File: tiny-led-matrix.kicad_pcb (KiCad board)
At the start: 4 copper layers, 89 x 85 mm, 998 parts, among them J1 TagConnect_TC2030_SWD, U1 STM32F030F4Px

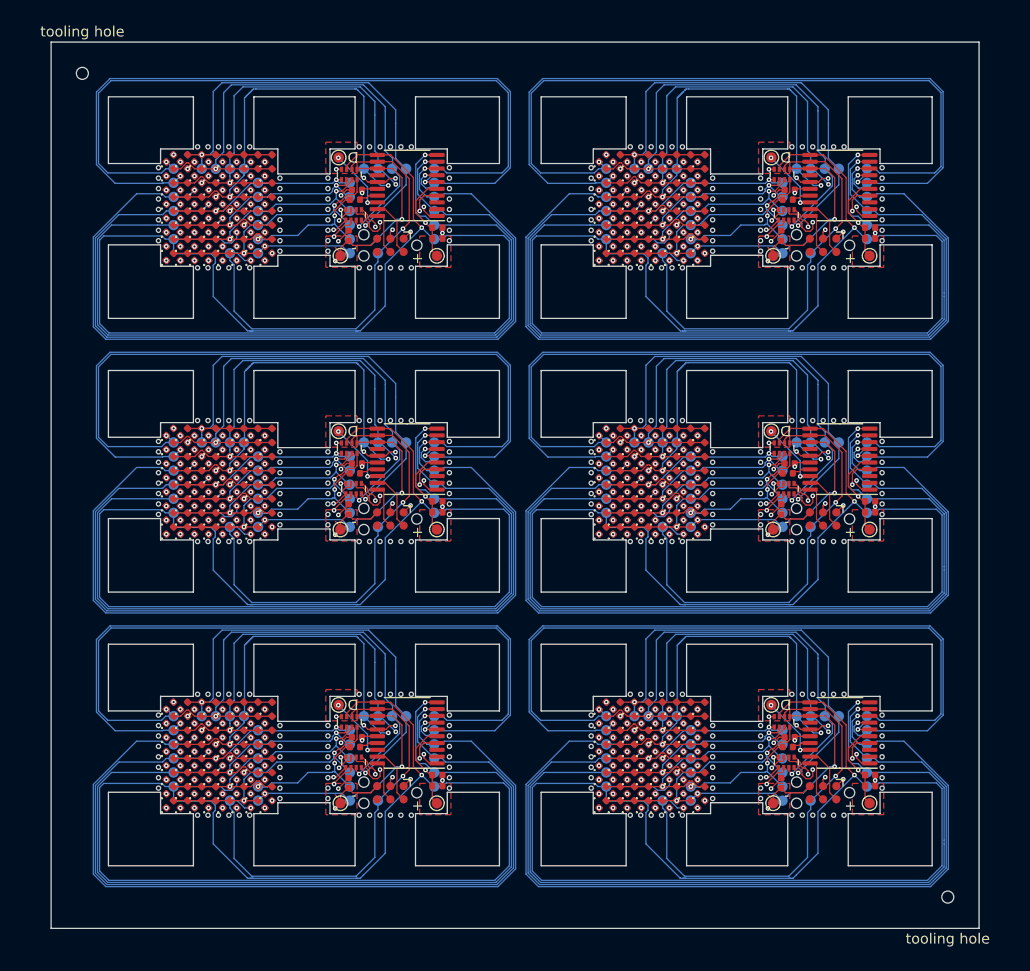
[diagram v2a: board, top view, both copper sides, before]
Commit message: Update board fab settings
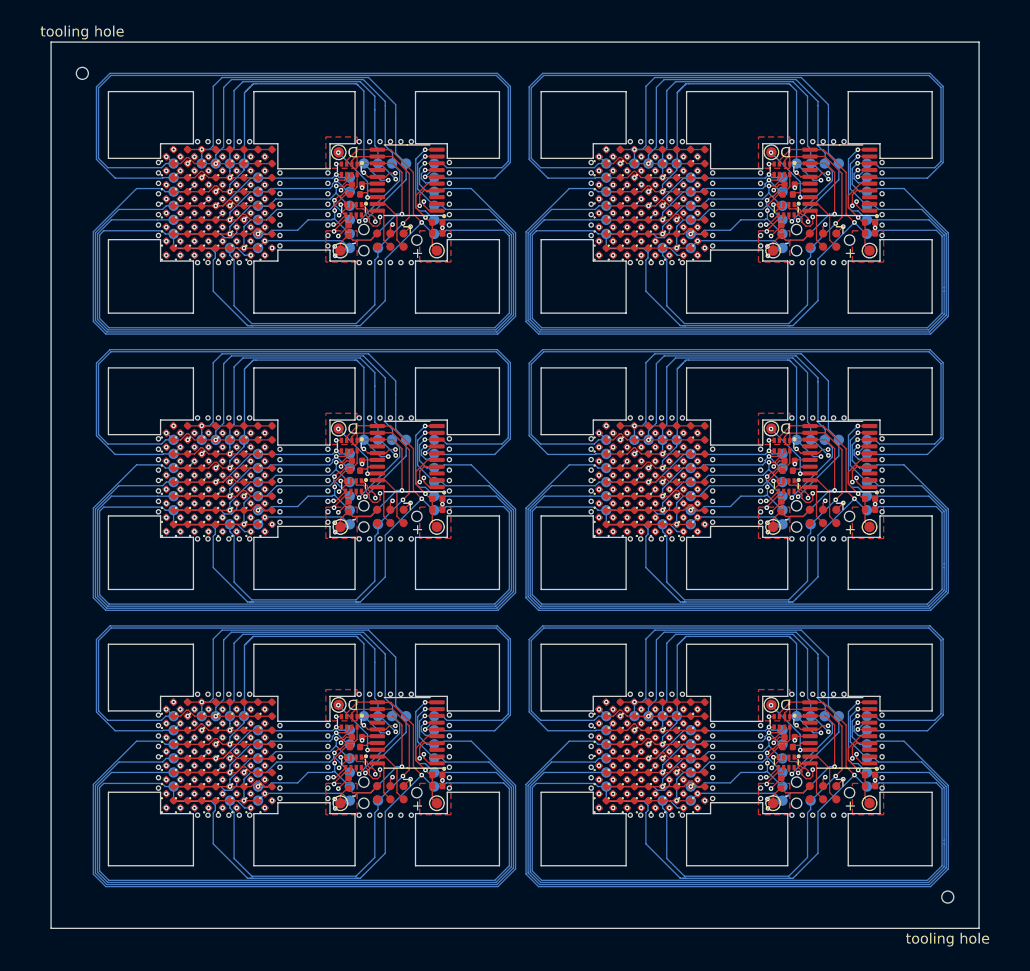
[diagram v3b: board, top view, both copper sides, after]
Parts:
- removed the C1 at (167.2, 81.5)
- removed the C1 at (167.2, 55.2)
- removed the C1 at (125.7, 55.2)
- removed the C1 at (125.7, 81.5)
- removed the C2 at (159.4, 76.8)
- removed the C2 at (159.4, 50.5)
- removed the C2 at (117.9, 50.5)
- removed the C2 at (117.9, 76.8)
- removed the C3 at (167.2, 54.1)
- removed the C3 at (167.2, 80.4)
- removed the C3 at (125.7, 54.1)
- removed the C3 at (125.7, 80.4)
- removed the C4 at (158.6, 81.2)
- removed the C4 at (158.6, 54.9)
- removed the C4 at (117.1, 54.9)
- removed the C4 at (117.1, 81.2)
- removed the D1 at (141.5, 73.8)
- removed the D1 at (141.5, 47.5)
- removed the D1 at (100.0, 47.5)
- removed the D1 at (100.0, 73.8)
- removed the D10 at (142.8, 48.9)
- removed the D10 at (142.8, 75.1)
- removed the D10 at (101.3, 48.9)
- removed the D10 at (101.3, 75.1)
- removed the D11 at (142.8, 50.2)
- removed the D11 at (142.8, 76.5)
- removed the D11 at (101.3, 50.2)
- removed the D11 at (101.3, 76.5)
- removed the D12 at (142.8, 77.8)
- removed the D12 at (142.8, 51.5)
- removed the D12 at (101.3, 51.5)
- removed the D12 at (101.3, 77.8)
- removed the D13 at (142.8, 52.9)
- removed the D13 at (142.8, 79.2)
- removed the D13 at (101.3, 52.9)
- removed the D13 at (101.3, 79.2)
- removed the D14 at (142.8, 54.2)
- removed the D14 at (142.8, 80.5)
- removed the D14 at (101.3, 54.2)
- removed the D14 at (101.3, 80.5)
- removed the D15 at (142.8, 55.6)
- removed the D15 at (142.8, 81.8)
- removed the D15 at (101.3, 55.6)
- removed the D15 at (101.3, 81.8)
- removed the D16 at (142.8, 57.0)
- removed the D16 at (142.8, 83.2)
- removed the D16 at (101.3, 57.0)
- removed the D16 at (101.3, 83.2)
- removed the D17 at (144.2, 47.5)
- removed the D17 at (144.2, 73.8)
- removed the D17 at (102.7, 47.5)
- removed the D17 at (102.7, 73.8)
- removed the D18 at (144.2, 48.9)
- removed the D18 at (144.2, 75.1)
- removed the D18 at (102.7, 48.9)
- removed the D18 at (102.7, 75.1)
- removed the D19 at (144.2, 76.5)
- removed the D19 at (144.2, 50.2)
- removed the D19 at (102.7, 50.2)
- removed the D19 at (102.7, 76.5)
- removed the D2 at (141.5, 75.1)
- removed the D2 at (141.5, 48.9)
- removed the D2 at (100.0, 48.9)
- removed the D2 at (100.0, 75.1)
- removed the D20 at (144.2, 77.8)
- removed the D20 at (144.2, 51.5)
- removed the D20 at (102.7, 51.5)
- removed the D20 at (102.7, 77.8)
- removed the D21 at (144.2, 79.2)
- removed the D21 at (144.2, 52.9)
- removed the D21 at (102.7, 52.9)
- removed the D21 at (102.7, 79.2)
- removed the D22 at (144.2, 54.2)
- removed the D22 at (144.2, 80.5)
- removed the D22 at (102.7, 54.2)
- removed the D22 at (102.7, 80.5)
- removed the D23 at (144.2, 81.8)
- removed the D23 at (144.2, 55.6)
- removed the D23 at (102.7, 55.6)
- removed the D23 at (102.7, 81.8)
- removed the D24 at (144.2, 57.0)
- removed the D24 at (144.2, 83.2)
- removed the D24 at (102.7, 57.0)
- removed the D24 at (102.7, 83.2)
- removed the D25 at (145.6, 73.8)
- removed the D25 at (145.6, 47.5)
- removed the D25 at (104.0, 47.5)
- removed the D25 at (104.0, 73.8)
- removed the D26 at (145.6, 48.9)
- removed the D26 at (145.6, 75.1)
- removed the D26 at (104.0, 48.9)
- removed the D26 at (104.0, 75.1)
- removed the D27 at (145.6, 50.2)
- removed the D27 at (145.6, 76.5)
- removed the D27 at (104.0, 50.2)
- removed the D27 at (104.0, 76.5)
- removed the D28 at (145.6, 77.8)
- removed the D28 at (145.6, 51.5)
- removed the D28 at (104.0, 51.5)
- removed the D28 at (104.0, 77.8)
- removed the D29 at (145.6, 79.2)
- removed the D29 at (145.6, 52.9)
- removed the D29 at (104.0, 52.9)
- removed the D29 at (104.0, 79.2)
- removed the D3 at (141.5, 76.5)
- removed the D3 at (141.5, 50.2)
- removed the D3 at (100.0, 50.2)
- removed the D3 at (100.0, 76.5)
- removed the D30 at (145.6, 80.5)
- removed the D30 at (145.6, 54.2)
- removed the D30 at (104.0, 54.2)
- removed the D30 at (104.0, 80.5)
- removed the D31 at (145.6, 81.8)
- removed the D31 at (145.6, 55.6)
- removed the D31 at (104.0, 55.6)
- removed the D31 at (104.0, 81.8)
- removed the D32 at (145.6, 83.2)
- removed the D32 at (145.6, 57.0)
- removed the D32 at (104.0, 57.0)
- removed the D32 at (104.0, 83.2)
- removed the D33 at (146.9, 73.8)
- removed the D33 at (146.9, 47.5)
- removed the D33 at (105.4, 47.5)
- removed the D33 at (105.4, 73.8)
- removed the D34 at (146.9, 48.9)
- removed the D34 at (146.9, 75.1)
- removed the D34 at (105.4, 48.9)
- removed the D34 at (105.4, 75.1)
- removed the D35 at (146.9, 50.2)
- removed the D35 at (146.9, 76.5)
- removed the D35 at (105.4, 50.2)
- removed the D35 at (105.4, 76.5)
- removed the D36 at (146.9, 77.8)
- removed the D36 at (146.9, 51.5)
- removed the D36 at (105.4, 51.5)
- removed the D36 at (105.4, 77.8)
- removed the D37 at (146.9, 79.2)
- removed the D37 at (146.9, 52.9)
- removed the D37 at (105.4, 52.9)
- removed the D37 at (105.4, 79.2)
- removed the D38 at (146.9, 80.5)
- removed the D38 at (146.9, 54.2)
- removed the D38 at (105.4, 54.2)
- removed the D38 at (105.4, 80.5)
- removed the D39 at (146.9, 81.8)
- removed the D39 at (146.9, 55.6)
- removed the D39 at (105.4, 55.6)
- removed the D39 at (105.4, 81.8)
- removed the D4 at (141.5, 51.5)
- removed the D4 at (141.5, 77.8)
- removed the D4 at (100.0, 51.5)
- removed the D4 at (100.0, 77.8)
- removed the D40 at (146.9, 83.2)
- removed the D40 at (146.9, 57.0)
- removed the D40 at (105.4, 57.0)
- removed the D40 at (105.4, 83.2)
- removed the D41 at (148.2, 47.5)
- removed the D41 at (148.2, 73.8)
- removed the D41 at (106.8, 47.5)
- removed the D41 at (106.8, 73.8)
- removed the D42 at (148.2, 48.9)
- removed the D42 at (148.2, 75.1)
- removed the D42 at (106.8, 48.9)
- removed the D42 at (106.8, 75.1)
- removed the D43 at (148.2, 50.2)
- removed the D43 at (148.2, 76.5)
- removed the D43 at (106.8, 50.2)
- removed the D43 at (106.8, 76.5)
- removed the D44 at (148.2, 77.8)
- removed the D44 at (148.2, 51.5)
- removed the D44 at (106.8, 51.5)
- removed the D44 at (106.8, 77.8)
- removed the D45 at (148.2, 52.9)
- removed the D45 at (148.2, 79.2)
- removed the D45 at (106.8, 52.9)
- removed the D45 at (106.8, 79.2)
- removed the D46 at (148.2, 80.5)
- removed the D46 at (148.2, 54.2)
- removed the D46 at (106.8, 54.2)
- removed the D46 at (106.8, 80.5)
- removed the D47 at (148.2, 81.8)
- removed the D47 at (148.2, 55.6)
- removed the D47 at (106.8, 55.6)
- removed the D47 at (106.8, 81.8)
- removed the D48 at (148.2, 83.2)
- removed the D48 at (148.2, 57.0)
- removed the D48 at (106.8, 57.0)
- removed the D48 at (106.8, 83.2)
- removed the D49 at (149.6, 47.5)
- removed the D49 at (149.6, 73.8)
- removed the D49 at (108.1, 47.5)
- removed the D49 at (108.1, 73.8)
- removed the D5 at (141.5, 52.9)
- removed the D5 at (141.5, 79.2)
- removed the D5 at (100.0, 52.9)
- removed the D5 at (100.0, 79.2)
- removed the D50 at (149.6, 48.9)
- removed the D50 at (149.6, 75.1)
- removed the D50 at (108.1, 48.9)
- removed the D50 at (108.1, 75.1)
- removed the D51 at (149.6, 50.2)
- removed the D51 at (149.6, 76.5)
- removed the D51 at (108.1, 50.2)
- removed the D51 at (108.1, 76.5)
- removed the D52 at (149.6, 51.5)
- removed the D52 at (149.6, 77.8)
- removed the D52 at (108.1, 51.5)
- removed the D52 at (108.1, 77.8)
- removed the D53 at (149.6, 52.9)
- removed the D53 at (149.6, 79.2)
- removed the D53 at (108.1, 52.9)
- removed the D53 at (108.1, 79.2)
- removed the D54 at (149.6, 80.5)
- removed the D54 at (149.6, 54.2)
- removed the D54 at (108.1, 54.2)
- removed the D54 at (108.1, 80.5)
- removed the D55 at (149.6, 81.8)
- removed the D55 at (149.6, 55.6)
- removed the D55 at (108.1, 55.6)
- removed the D55 at (108.1, 81.8)
- removed the D56 at (149.6, 83.2)
- removed the D56 at (149.6, 57.0)
- removed the D56 at (108.1, 57.0)
- removed the D56 at (108.1, 83.2)
- removed the D57 at (150.9, 47.5)
- removed the D57 at (150.9, 73.8)
- removed the D57 at (109.5, 47.5)
- removed the D57 at (109.5, 73.8)
- removed the D58 at (150.9, 48.9)
- removed the D58 at (150.9, 75.1)
- removed the D58 at (109.5, 48.9)
- removed the D58 at (109.5, 75.1)
- removed the D59 at (150.9, 50.2)
- removed the D59 at (150.9, 76.5)
- removed the D59 at (109.5, 50.2)
- removed the D59 at (109.5, 76.5)
- removed the D6 at (141.5, 54.2)
- removed the D6 at (141.5, 80.5)
- removed the D6 at (100.0, 54.2)
- removed the D6 at (100.0, 80.5)
- removed the D60 at (150.9, 77.8)
- removed the D60 at (150.9, 51.5)
- removed the D60 at (109.5, 51.5)
- removed the D60 at (109.5, 77.8)
- removed the D61 at (150.9, 52.9)
- removed the D61 at (150.9, 79.2)
- removed the D61 at (109.5, 52.9)
- removed the D61 at (109.5, 79.2)
- removed the D62 at (150.9, 80.5)
- removed the D62 at (150.9, 54.2)
- removed the D62 at (109.5, 54.2)
- removed the D62 at (109.5, 80.5)
- removed the D63 at (150.9, 81.8)
- removed the D63 at (150.9, 55.6)
- removed the D63 at (109.5, 55.6)
- removed the D63 at (109.5, 81.8)
- removed the D64 at (150.9, 83.2)
- removed the D64 at (150.9, 57.0)
- removed the D64 at (109.5, 57.0)
- removed the D64 at (109.5, 83.2)
- removed the D7 at (141.5, 81.8)
- removed the D7 at (141.5, 55.6)
- removed the D7 at (100.0, 55.6)
- removed the D7 at (100.0, 81.8)
- removed the D8 at (141.5, 57.0)
- removed the D8 at (141.5, 83.2)
- removed the D8 at (100.0, 57.0)
- removed the D8 at (100.0, 83.2)
- removed the D9 at (142.8, 73.8)
- removed the D9 at (142.8, 47.5)
- removed the D9 at (101.3, 47.5)
- removed the D9 at (101.3, 73.8)
- removed the J1 at (162.6, 55.8)
- removed the J1 at (162.6, 82.1)
- removed the J1 at (121.1, 55.8)
- removed the J1 at (121.1, 82.1)
- removed the R1 at (159.2, 77.7)
- removed the R1 at (159.2, 51.5)
- removed the R1 at (117.8, 51.5)
- removed the R1 at (117.8, 77.7)
- removed the REF** at (161.7, 72.7)
- removed the REF** at (162.7, 46.4)
- removed the REF** at (168.3, 52.4)
- removed the REF** at (147.2, 84.2)
- removed the REF** at (163.7, 58.0)
- removed the REF** at (146.2, 46.4)
- removed the REF** at (162.7, 58.0)
- removed the REF** at (163.7, 46.4)
- removed the REF** at (161.7, 46.4)
- removed the REF** at (148.2, 58.0)
- removed the REF** at (160.7, 46.4)
- removed the REF** at (144.2, 46.4)
- removed the REF** at (147.2, 46.4)
- removed the REF** at (161.7, 58.0)
- removed the REF** at (160.7, 58.0)
- removed the REF** at (164.7, 58.0)
- removed the REF** at (159.7, 58.0)
- removed the REF** at (156.7, 81.7)
- removed the REF** at (152.1, 79.7)
- removed the REF** at (140.4, 51.4)
- removed the REF** at (146.2, 58.0)
- removed the REF** at (152.1, 49.4)
- removed the REF** at (152.1, 55.4)
- removed the REF** at (152.1, 54.4)
- removed the REF** at (152.1, 53.4)
- removed the REF** at (152.1, 56.4)
- removed the REF** at (156.7, 76.7)
- removed the REF** at (152.1, 50.4)
- removed the REF** at (152.1, 51.4)
- removed the REF** at (140.4, 81.7)
- removed the REF** at (156.7, 78.7)
- removed the REF** at (168.3, 55.4)
- removed the REF** at (147.2, 58.0)
- removed the REF** at (152.1, 82.7)
- removed the REF** at (164.7, 46.4)
- removed the REF** at (168.3, 50.4)
- removed the REF** at (168.3, 53.4)
- removed the REF** at (145.2, 58.0)
- removed the REF** at (168.3, 48.4)
- removed the REF** at (168.3, 49.4)
- removed the REF** at (152.1, 77.7)
- removed the REF** at (159.7, 46.4)
- removed the REF** at (140.4, 52.4)
- removed the REF** at (140.4, 49.4)
- removed the REF** at (140.4, 50.4)
- removed the REF** at (156.7, 56.4)
- removed the REF** at (156.7, 50.4)
- removed the REF** at (156.7, 51.4)
- removed the REF** at (168.3, 54.4)
- removed the REF** at (140.4, 54.4)
- removed the REF** at (140.4, 55.4)
- removed the REF** at (168.3, 78.7)
- removed the REF** at (156.7, 52.4)
- removed the REF** at (168.3, 51.4)
- removed the REF** at (144.2, 58.0)
- removed the REF** at (156.7, 55.4)
- removed the REF** at (168.3, 77.7)
- removed the REF** at (156.7, 79.7)
- removed the REF** at (159.7, 72.7)
- removed the REF** at (156.7, 80.7)
- removed the REF** at (115.2, 49.4)
- removed the REF** at (126.8, 51.4)
- removed the REF** at (115.2, 52.4)
- removed the REF** at (98.9, 55.4)
- removed the REF** at (98.9, 54.4)
- removed the REF** at (126.8, 54.4)
- removed the REF** at (115.2, 51.4)
- removed the REF** at (115.2, 50.4)
- removed the REF** at (115.2, 56.4)
- removed the REF** at (148.2, 84.2)
- removed the REF** at (98.9, 50.4)
- removed the REF** at (98.9, 49.4)
- removed the REF** at (98.9, 52.4)
- removed the REF** at (118.2, 46.4)
- removed the REF** at (126.8, 49.4)
- removed the REF** at (126.8, 48.4)
- removed the REF** at (103.7, 58.0)
- removed the REF** at (126.8, 50.4)
- removed the REF** at (123.2, 46.4)
- removed the REF** at (107.7, 58.0)
- removed the REF** at (160.7, 72.7)
- removed the REF** at (115.2, 53.4)
- removed the REF** at (115.2, 54.4)
- removed the REF** at (115.2, 55.4)
- removed the REF** at (107.7, 46.4)
- removed the REF** at (98.9, 48.4)
- removed the REF** at (103.7, 46.4)
- removed the REF** at (104.7, 46.4)
- removed the REF** at (122.2, 58.0)
- removed the REF** at (106.7, 46.4)
- removed the REF** at (110.5, 52.4)
- removed the REF** at (144.2, 72.7)
- removed the REF** at (110.5, 51.4)
- removed the REF** at (110.5, 50.4)
- removed the REF** at (110.5, 56.4)
- removed the REF** at (110.5, 53.4)
- removed the REF** at (110.5, 54.4)
- removed the REF** at (110.5, 55.4)
- removed the REF** at (110.5, 49.4)
- removed the REF** at (104.7, 58.0)
- removed the REF** at (118.2, 58.0)
- removed the REF** at (123.2, 58.0)
- removed the REF** at (152.1, 78.7)
- removed the REF** at (119.2, 58.0)
- removed the REF** at (120.2, 58.0)
- removed the REF** at (105.7, 46.4)
- removed the REF** at (102.7, 46.4)
- removed the REF** at (119.2, 46.4)
- removed the REF** at (106.7, 58.0)
- removed the REF** at (120.2, 46.4)
- removed the REF** at (122.2, 46.4)
- removed the REF** at (121.2, 58.0)
- removed the REF** at (98.9, 53.4)
- removed the REF** at (148.2, 72.7)
- removed the REF** at (102.7, 58.0)
- removed the REF** at (126.8, 53.4)
- removed the REF** at (105.7, 58.0)
- removed the REF** at (126.8, 55.4)
- removed the REF** at (98.9, 51.4)
- removed the REF** at (126.8, 52.4)
- removed the REF** at (121.2, 46.4)
- removed the REF** at (115.2, 75.7)
- removed the REF** at (126.8, 77.7)
- removed the REF** at (115.2, 78.7)
- removed the REF** at (140.4, 78.7)
- removed the REF** at (98.9, 81.7)
- removed the REF** at (98.9, 80.7)
- removed the REF** at (126.8, 80.7)
- removed the REF** at (115.2, 77.7)
- removed the REF** at (115.2, 76.7)
- removed the REF** at (115.2, 82.7)
- removed the REF** at (98.9, 76.7)
- removed the REF** at (98.9, 75.7)
- removed the REF** at (98.9, 78.7)
- removed the REF** at (118.2, 72.7)
- removed the REF** at (163.7, 72.7)
- removed the REF** at (126.8, 75.7)
- removed the REF** at (126.8, 74.7)
- removed the REF** at (103.7, 84.2)
- removed the REF** at (126.8, 76.7)
- removed the REF** at (123.2, 72.7)
- removed the REF** at (107.7, 84.2)
- removed the REF** at (115.2, 79.7)
- removed the REF** at (115.2, 80.7)
- removed the REF** at (115.2, 81.7)
- removed the REF** at (107.7, 72.7)
- removed the REF** at (147.2, 72.7)
- removed the REF** at (98.9, 74.7)
- removed the REF** at (103.7, 72.7)
- removed the REF** at (104.7, 72.7)
- removed the REF** at (122.2, 84.2)
- removed the REF** at (106.7, 72.7)
- removed the REF** at (110.5, 78.7)
- removed the REF** at (110.5, 77.7)
- removed the REF** at (110.5, 76.7)
- removed the REF** at (110.5, 82.7)
- removed the REF** at (110.5, 79.7)
- removed the REF** at (161.7, 84.2)
- removed the REF** at (110.5, 80.7)
- removed the REF** at (110.5, 81.7)
- removed the REF** at (110.5, 75.7)
- removed the REF** at (104.7, 84.2)
- removed the REF** at (118.2, 84.2)
- removed the REF** at (123.2, 84.2)
- removed the REF** at (119.2, 84.2)
- removed the REF** at (120.2, 84.2)
- removed the REF** at (105.7, 72.7)
- removed the REF** at (102.7, 72.7)
- removed the REF** at (160.7, 84.2)
- removed the REF** at (119.2, 72.7)
- removed the REF** at (106.7, 84.2)
- removed the REF** at (120.2, 72.7)
- removed the REF** at (122.2, 72.7)
- removed the REF** at (121.2, 84.2)
- removed the REF** at (98.9, 79.7)
- removed the REF** at (102.7, 84.2)
- removed the REF** at (126.8, 79.7)
- removed the REF** at (105.7, 84.2)
- removed the REF** at (126.8, 81.7)
- removed the REF** at (168.3, 79.7)
- removed the REF** at (98.9, 77.7)
- removed the REF** at (126.8, 78.7)
- removed the REF** at (121.2, 72.7)
- removed the REF** at (145.2, 46.4)
- removed the REF** at (164.7, 84.2)
- removed the REF** at (156.7, 54.4)
- removed the REF** at (152.1, 52.4)
- removed the REF** at (144.2, 84.2)
- removed the REF** at (140.4, 79.7)
- removed the REF** at (156.7, 75.7)
- removed the REF** at (168.3, 75.7)
- removed the REF** at (163.7, 84.2)
- removed the REF** at (159.7, 84.2)
- removed the REF** at (156.7, 77.7)
- removed the REF** at (140.4, 75.7)
- removed the REF** at (156.7, 49.4)
- removed the REF** at (140.4, 76.7)
- removed the REF** at (146.2, 84.2)
- removed the REF** at (146.2, 72.7)
- removed the REF** at (168.3, 80.7)
- removed the REF** at (152.1, 75.7)
- removed the REF** at (149.2, 84.2)
- removed the REF** at (164.7, 72.7)
- removed the REF** at (168.3, 76.7)
- removed the REF** at (145.2, 84.2)
- removed the REF** at (168.3, 74.7)
- removed the REF** at (148.2, 46.4)
- removed the REF** at (156.7, 53.4)
- removed the REF** at (140.4, 77.7)
- removed the REF** at (168.3, 81.7)
- removed the REF** at (140.4, 48.4)
- removed the REF** at (149.2, 46.4)
- removed the REF** at (162.7, 72.7)
- removed the REF** at (156.7, 82.7)
- removed the REF** at (149.2, 58.0)
- removed the REF** at (162.7, 84.2)
- removed the REF** at (152.1, 81.7)
- removed the REF** at (145.2, 72.7)
- removed the REF** at (140.4, 80.7)
- removed the REF** at (140.4, 74.7)
- removed the REF** at (149.2, 72.7)
- removed the REF** at (140.4, 53.4)
- removed the REF** at (152.1, 76.7)
- removed the REF** at (152.1, 80.7)
- removed the RN1 at (159.1, 79.2)
- removed the RN1 at (159.1, 52.9)
- removed the RN1 at (117.6, 52.9)
- removed the RN1 at (117.6, 79.2)
- removed the RN2 at (158.7, 75.3)
- removed the RN2 at (158.7, 49.0)
- removed the RN2 at (117.2, 49.0)
- removed the RN2 at (117.2, 75.3)
- removed the TP1 at (144.6, 74.8)
- removed the TP1 at (144.6, 48.5)
- removed the TP1 at (103.0, 48.5)
- removed the TP1 at (103.0, 74.8)
- removed the TP10 at (141.8, 74.8)
- removed the TP10 at (141.8, 48.5)
- removed the TP10 at (100.3, 48.5)
- removed the TP10 at (100.3, 74.8)
- removed the TP11 at (141.8, 76.1)
- removed the TP11 at (141.8, 49.9)
- removed the TP11 at (100.3, 49.9)
- removed the TP11 at (100.3, 76.1)
- removed the TP12 at (141.8, 77.5)
- removed the TP12 at (141.8, 51.2)
- removed the TP12 at (100.3, 51.2)
- removed the TP12 at (100.3, 77.5)
- removed the TP13 at (141.8, 52.5)
- removed the TP13 at (141.8, 78.8)
- removed the TP13 at (100.3, 52.5)
- removed the TP13 at (100.3, 78.8)
- removed the TP14 at (141.8, 53.9)
- removed the TP14 at (141.8, 80.2)
- removed the TP14 at (100.3, 53.9)
- removed the TP14 at (100.3, 80.2)
- removed the TP15 at (141.8, 55.2)
- removed the TP15 at (141.8, 81.5)
- removed the TP15 at (100.3, 55.2)
- removed the TP15 at (100.3, 81.5)
- removed the TP16 at (147.2, 56.6)
- removed the TP16 at (147.2, 82.8)
- removed the TP16 at (105.8, 56.6)
- removed the TP16 at (105.8, 82.8)
- removed the TP17 at (149.9, 82.8)
- removed the TP17 at (149.9, 56.6)
- removed the TP17 at (108.5, 56.6)
- removed the TP17 at (108.5, 82.8)
- removed the TP18 at (164.2, 48.5)
- removed the TP18 at (164.2, 74.8)
- removed the TP18 at (122.7, 48.5)
- removed the TP18 at (122.7, 74.8)
- removed the TP19 at (162.8, 48.5)
- removed the TP19 at (162.8, 74.8)
- removed the TP19 at (121.3, 48.5)
- removed the TP19 at (121.3, 74.8)
- removed the TP2 at (145.9, 48.5)
- removed the TP2 at (145.9, 74.8)
- removed the TP2 at (104.4, 48.5)
- removed the TP2 at (104.4, 74.8)
- removed the TP20 at (161.4, 74.8)
- removed the TP20 at (161.4, 48.5)
- removed the TP20 at (120.0, 48.5)
- removed the TP20 at (120.0, 74.8)
- removed the TP21 at (160.1, 74.8)
- removed the TP21 at (160.1, 48.5)
- removed the TP21 at (118.6, 48.5)
- removed the TP21 at (118.6, 74.8)
- removed the TP22 at (158.8, 76.1)
- removed the TP22 at (158.8, 49.9)
- removed the TP22 at (117.2, 49.9)
- removed the TP22 at (117.2, 76.1)
- removed the TP23 at (158.8, 77.5)
- removed the TP23 at (158.8, 51.2)
- removed the TP23 at (117.2, 51.2)
- removed the TP23 at (117.2, 77.5)
- removed the TP24 at (158.8, 78.8)
- removed the TP24 at (158.8, 52.5)
- removed the TP24 at (117.2, 52.5)
- removed the TP24 at (117.2, 78.8)
- removed the TP25 at (158.8, 80.2)
- removed the TP25 at (158.8, 53.9)
- removed the TP25 at (117.2, 53.9)
- removed the TP25 at (117.2, 80.2)
- removed the TP26 at (158.8, 81.5)
- removed the TP26 at (158.8, 55.2)
- removed the TP26 at (117.3, 55.2)
- removed the TP26 at (117.3, 81.5)
- removed the TP27 at (166.8, 74.8)
- removed the TP27 at (166.8, 48.5)
- removed the TP27 at (125.3, 48.5)
- removed the TP27 at (125.3, 74.8)
- removed the TP28 at (166.8, 76.1)
- removed the TP28 at (166.8, 49.9)
- removed the TP28 at (125.3, 49.9)
- removed the TP28 at (125.3, 76.1)
- removed the TP29 at (166.8, 77.5)
- removed the TP29 at (166.8, 51.2)
- removed the TP29 at (125.3, 51.2)
- removed the TP29 at (125.3, 77.5)
- removed the TP3 at (147.2, 48.5)
- removed the TP3 at (147.2, 74.8)
- removed the TP3 at (105.7, 48.5)
- removed the TP3 at (105.7, 74.8)
- removed the TP30 at (166.8, 52.5)
- removed the TP30 at (166.8, 78.8)
- removed the TP30 at (125.3, 52.5)
- removed the TP30 at (125.3, 78.8)
- removed the TP31 at (166.8, 53.9)
- removed the TP31 at (166.8, 80.2)
- removed the TP31 at (125.3, 53.9)
- removed the TP31 at (125.3, 80.2)
- removed the TP32 at (166.8, 81.5)
- removed the TP32 at (166.8, 55.2)
- removed the TP32 at (125.3, 55.2)
- removed the TP32 at (125.3, 81.5)
- removed the TP33 at (161.4, 82.8)
- removed the TP33 at (161.4, 56.6)
- removed the TP33 at (120.0, 56.6)
- removed the TP33 at (120.0, 82.8)
- removed the TP34 at (158.8, 82.8)
- removed the TP34 at (158.8, 56.6)
- removed the TP34 at (117.3, 56.6)
- removed the TP34 at (117.3, 82.8)
- removed the TP35 at (167.1, 56.9)
- removed the TP35 at (167.1, 83.1)
- removed the TP35 at (125.6, 56.9)
- removed the TP35 at (125.6, 83.1)
- removed the TP36 at (157.7, 47.4)
- removed the TP36 at (157.7, 73.7)
- removed the TP36 at (116.2, 47.4)
- removed the TP36 at (116.2, 73.7)
- removed the TP37 at (157.8, 83.1)
- removed the TP37 at (157.8, 56.9)
- removed the TP37 at (116.3, 56.9)
- removed the TP37 at (116.3, 83.1)
- removed the TP4 at (148.6, 74.8)
- removed the TP4 at (148.6, 48.5)
- removed the TP4 at (107.1, 48.5)
- removed the TP4 at (107.1, 74.8)
- removed the TP5 at (149.9, 49.9)
- removed the TP5 at (149.9, 76.1)
- removed the TP5 at (108.5, 49.9)
- removed the TP5 at (108.5, 76.1)
- removed the TP6 at (149.9, 51.2)
- removed the TP6 at (149.9, 77.5)
- removed the TP6 at (108.5, 51.2)
- removed the TP6 at (108.5, 77.5)
- removed the TP7 at (149.9, 52.5)
- removed the TP7 at (149.9, 78.8)
- removed the TP7 at (108.5, 52.5)
- removed the TP7 at (108.5, 78.8)
- removed the TP8 at (149.9, 53.9)
- removed the TP8 at (149.9, 80.2)
- removed the TP8 at (108.5, 53.9)
- removed the TP8 at (108.5, 80.2)
- removed the TP9 at (149.9, 81.5)
- removed the TP9 at (149.9, 55.2)
- removed the TP9 at (108.5, 55.2)
- removed the TP9 at (108.5, 81.5)
- removed the U1 at (164.2, 76.3)
- removed the U1 at (164.2, 50.1)
- removed the U1 at (122.8, 50.1)
- removed the U1 at (122.8, 76.3)
- added C1: 10uF, Capacitor_SMD:C_0402_1005Metric, F.Cu at (167.2, 54.7)
- added C1: 10uF, Capacitor_SMD:C_0402_1005Metric, F.Cu at (125.7, 54.7)
- added C1: 10uF, Capacitor_SMD:C_0402_1005Metric, F.Cu at (167.2, 81.2)
- added C1: 10uF, Capacitor_SMD:C_0402_1005Metric, F.Cu at (125.7, 81.2)
- added C2: 100nF, Capacitor_SMD:C_0402_1005Metric, F.Cu at (159.4, 50.0)
- added C2: 100nF, Capacitor_SMD:C_0402_1005Metric, F.Cu at (117.9, 50.0)
- added C2: 100nF, Capacitor_SMD:C_0402_1005Metric, F.Cu at (159.4, 76.5)
- added C2: 100nF, Capacitor_SMD:C_0402_1005Metric, F.Cu at (117.9, 76.5)
- added C3: 100nF, Capacitor_SMD:C_0402_1005Metric, F.Cu at (167.2, 53.6)
- added C3: 100nF, Capacitor_SMD:C_0402_1005Metric, F.Cu at (125.7, 53.6)
- added C3: 100nF, Capacitor_SMD:C_0402_1005Metric, F.Cu at (167.2, 80.2)
- added C3: 100nF, Capacitor_SMD:C_0402_1005Metric, F.Cu at (125.7, 80.2)
- added C4: 100nF, Capacitor_SMD:C_0402_1005Metric, F.Cu at (158.6, 54.4)
- added C4: 100nF, Capacitor_SMD:C_0402_1005Metric, F.Cu at (117.1, 54.4)
- added C4: 100nF, Capacitor_SMD:C_0402_1005Metric, F.Cu at (158.6, 80.9)
- added C4: 100nF, Capacitor_SMD:C_0402_1005Metric, F.Cu at (117.1, 80.9)
- added D1: LED, LED_SMD:LED_0402_1005Metric, F.Cu at (141.5, 47.0)
- added D1: LED, LED_SMD:LED_0402_1005Metric, F.Cu at (100.0, 47.0)
- added D1: LED, LED_SMD:LED_0402_1005Metric, F.Cu at (141.5, 73.5)
- added D1: LED, LED_SMD:LED_0402_1005Metric, F.Cu at (100.0, 73.5)
- added D10: LED, LED_SMD:LED_0402_1005Metric, F.Cu at (142.8, 48.4)
- added D10: LED, LED_SMD:LED_0402_1005Metric, F.Cu at (101.3, 48.4)
- added D10: LED, LED_SMD:LED_0402_1005Metric, F.Cu at (142.8, 74.8)
- added D10: LED, LED_SMD:LED_0402_1005Metric, F.Cu at (101.3, 74.8)
- added D11: LED, LED_SMD:LED_0402_1005Metric, F.Cu at (142.8, 49.7)
- added D11: LED, LED_SMD:LED_0402_1005Metric, F.Cu at (101.3, 49.7)
- added D11: LED, LED_SMD:LED_0402_1005Metric, F.Cu at (142.8, 76.2)
- added D11: LED, LED_SMD:LED_0402_1005Metric, F.Cu at (101.3, 76.2)
- added D12: LED, LED_SMD:LED_0402_1005Metric, F.Cu at (142.8, 51.0)
- added D12: LED, LED_SMD:LED_0402_1005Metric, F.Cu at (101.3, 51.0)
- added D12: LED, LED_SMD:LED_0402_1005Metric, F.Cu at (142.8, 77.5)
- added D12: LED, LED_SMD:LED_0402_1005Metric, F.Cu at (101.3, 77.5)
- added D13: LED, LED_SMD:LED_0402_1005Metric, F.Cu at (142.8, 52.4)
- added D13: LED, LED_SMD:LED_0402_1005Metric, F.Cu at (101.3, 52.4)
- added D13: LED, LED_SMD:LED_0402_1005Metric, F.Cu at (142.8, 78.9)
- added D13: LED, LED_SMD:LED_0402_1005Metric, F.Cu at (101.3, 78.9)
- added D14: LED, LED_SMD:LED_0402_1005Metric, F.Cu at (142.8, 53.8)
- added D14: LED, LED_SMD:LED_0402_1005Metric, F.Cu at (101.3, 53.8)
- added D14: LED, LED_SMD:LED_0402_1005Metric, F.Cu at (142.8, 80.2)
- added D14: LED, LED_SMD:LED_0402_1005Metric, F.Cu at (101.3, 80.2)
- added D15: LED, LED_SMD:LED_0402_1005Metric, F.Cu at (142.8, 55.1)
- added D15: LED, LED_SMD:LED_0402_1005Metric, F.Cu at (101.3, 55.1)
- added D15: LED, LED_SMD:LED_0402_1005Metric, F.Cu at (142.8, 81.6)
- added D15: LED, LED_SMD:LED_0402_1005Metric, F.Cu at (101.3, 81.6)
- added D16: LED, LED_SMD:LED_0402_1005Metric, F.Cu at (142.8, 56.5)
- added D16: LED, LED_SMD:LED_0402_1005Metric, F.Cu at (101.3, 56.5)
- added D16: LED, LED_SMD:LED_0402_1005Metric, F.Cu at (142.8, 83.0)
- added D16: LED, LED_SMD:LED_0402_1005Metric, F.Cu at (101.3, 83.0)
- added D17: LED, LED_SMD:LED_0402_1005Metric, F.Cu at (144.2, 47.0)
- added D17: LED, LED_SMD:LED_0402_1005Metric, F.Cu at (102.7, 47.0)
- added D17: LED, LED_SMD:LED_0402_1005Metric, F.Cu at (144.2, 73.5)
- added D17: LED, LED_SMD:LED_0402_1005Metric, F.Cu at (102.7, 73.5)
- added D18: LED, LED_SMD:LED_0402_1005Metric, F.Cu at (144.2, 48.4)
- added D18: LED, LED_SMD:LED_0402_1005Metric, F.Cu at (102.7, 48.4)
- added D18: LED, LED_SMD:LED_0402_1005Metric, F.Cu at (144.2, 74.8)
- added D18: LED, LED_SMD:LED_0402_1005Metric, F.Cu at (102.7, 74.8)
- added D19: LED, LED_SMD:LED_0402_1005Metric, F.Cu at (144.2, 49.7)
- added D19: LED, LED_SMD:LED_0402_1005Metric, F.Cu at (102.7, 49.7)
- added D19: LED, LED_SMD:LED_0402_1005Metric, F.Cu at (144.2, 76.2)
- added D19: LED, LED_SMD:LED_0402_1005Metric, F.Cu at (102.7, 76.2)
- added D2: LED, LED_SMD:LED_0402_1005Metric, F.Cu at (141.5, 48.4)
- added D2: LED, LED_SMD:LED_0402_1005Metric, F.Cu at (100.0, 48.4)
- added D2: LED, LED_SMD:LED_0402_1005Metric, F.Cu at (141.5, 74.8)
- added D2: LED, LED_SMD:LED_0402_1005Metric, F.Cu at (100.0, 74.8)
- added D20: LED, LED_SMD:LED_0402_1005Metric, F.Cu at (144.2, 51.0)
- added D20: LED, LED_SMD:LED_0402_1005Metric, F.Cu at (102.7, 51.0)
- added D20: LED, LED_SMD:LED_0402_1005Metric, F.Cu at (144.2, 77.5)
- added D20: LED, LED_SMD:LED_0402_1005Metric, F.Cu at (102.7, 77.5)
- added D21: LED, LED_SMD:LED_0402_1005Metric, F.Cu at (144.2, 52.4)
- added D21: LED, LED_SMD:LED_0402_1005Metric, F.Cu at (102.7, 52.4)
- added D21: LED, LED_SMD:LED_0402_1005Metric, F.Cu at (144.2, 78.9)
- added D21: LED, LED_SMD:LED_0402_1005Metric, F.Cu at (102.7, 78.9)
- added D22: LED, LED_SMD:LED_0402_1005Metric, F.Cu at (144.2, 53.8)
- added D22: LED, LED_SMD:LED_0402_1005Metric, F.Cu at (102.7, 53.8)
- added D22: LED, LED_SMD:LED_0402_1005Metric, F.Cu at (144.2, 80.2)
- added D22: LED, LED_SMD:LED_0402_1005Metric, F.Cu at (102.7, 80.2)
- added D23: LED, LED_SMD:LED_0402_1005Metric, F.Cu at (144.2, 55.1)
- added D23: LED, LED_SMD:LED_0402_1005Metric, F.Cu at (102.7, 55.1)
- added D23: LED, LED_SMD:LED_0402_1005Metric, F.Cu at (144.2, 81.6)
- added D23: LED, LED_SMD:LED_0402_1005Metric, F.Cu at (102.7, 81.6)
- added D24: LED, LED_SMD:LED_0402_1005Metric, F.Cu at (144.2, 56.5)
- added D24: LED, LED_SMD:LED_0402_1005Metric, F.Cu at (102.7, 56.5)
- added D24: LED, LED_SMD:LED_0402_1005Metric, F.Cu at (144.2, 83.0)
- added D24: LED, LED_SMD:LED_0402_1005Metric, F.Cu at (102.7, 83.0)
- added D25: LED, LED_SMD:LED_0402_1005Metric, F.Cu at (145.6, 47.0)
- added D25: LED, LED_SMD:LED_0402_1005Metric, F.Cu at (104.0, 47.0)
- added D25: LED, LED_SMD:LED_0402_1005Metric, F.Cu at (145.6, 73.5)
- added D25: LED, LED_SMD:LED_0402_1005Metric, F.Cu at (104.0, 73.5)
- added D26: LED, LED_SMD:LED_0402_1005Metric, F.Cu at (145.6, 48.4)
- added D26: LED, LED_SMD:LED_0402_1005Metric, F.Cu at (104.0, 48.4)
- added D26: LED, LED_SMD:LED_0402_1005Metric, F.Cu at (145.6, 74.8)
- added D26: LED, LED_SMD:LED_0402_1005Metric, F.Cu at (104.0, 74.8)
- added D27: LED, LED_SMD:LED_0402_1005Metric, F.Cu at (145.6, 49.7)
- added D27: LED, LED_SMD:LED_0402_1005Metric, F.Cu at (104.0, 49.7)
- added D27: LED, LED_SMD:LED_0402_1005Metric, F.Cu at (145.6, 76.2)
- added D27: LED, LED_SMD:LED_0402_1005Metric, F.Cu at (104.0, 76.2)
- added D28: LED, LED_SMD:LED_0402_1005Metric, F.Cu at (145.6, 51.0)
- added D28: LED, LED_SMD:LED_0402_1005Metric, F.Cu at (104.0, 51.0)
- added D28: LED, LED_SMD:LED_0402_1005Metric, F.Cu at (145.6, 77.5)
- added D28: LED, LED_SMD:LED_0402_1005Metric, F.Cu at (104.0, 77.5)
- added D29: LED, LED_SMD:LED_0402_1005Metric, F.Cu at (145.6, 52.4)
- added D29: LED, LED_SMD:LED_0402_1005Metric, F.Cu at (104.0, 52.4)
- added D29: LED, LED_SMD:LED_0402_1005Metric, F.Cu at (145.6, 78.9)
- added D29: LED, LED_SMD:LED_0402_1005Metric, F.Cu at (104.0, 78.9)
- added D3: LED, LED_SMD:LED_0402_1005Metric, F.Cu at (141.5, 49.7)
- added D3: LED, LED_SMD:LED_0402_1005Metric, F.Cu at (100.0, 49.7)
- added D3: LED, LED_SMD:LED_0402_1005Metric, F.Cu at (141.5, 76.2)
- added D3: LED, LED_SMD:LED_0402_1005Metric, F.Cu at (100.0, 76.2)
- added D30: LED, LED_SMD:LED_0402_1005Metric, F.Cu at (145.6, 53.8)
- added D30: LED, LED_SMD:LED_0402_1005Metric, F.Cu at (104.0, 53.8)
- added D30: LED, LED_SMD:LED_0402_1005Metric, F.Cu at (145.6, 80.2)
- added D30: LED, LED_SMD:LED_0402_1005Metric, F.Cu at (104.0, 80.2)
- added D31: LED, LED_SMD:LED_0402_1005Metric, F.Cu at (145.6, 55.1)
- added D31: LED, LED_SMD:LED_0402_1005Metric, F.Cu at (104.0, 55.1)
- added D31: LED, LED_SMD:LED_0402_1005Metric, F.Cu at (145.6, 81.6)
- added D31: LED, LED_SMD:LED_0402_1005Metric, F.Cu at (104.0, 81.6)
- added D32: LED, LED_SMD:LED_0402_1005Metric, F.Cu at (145.6, 56.5)
- added D32: LED, LED_SMD:LED_0402_1005Metric, F.Cu at (104.0, 56.5)
- added D32: LED, LED_SMD:LED_0402_1005Metric, F.Cu at (145.6, 83.0)
- added D32: LED, LED_SMD:LED_0402_1005Metric, F.Cu at (104.0, 83.0)
- added D33: LED, LED_SMD:LED_0402_1005Metric, F.Cu at (146.9, 47.0)
- added D33: LED, LED_SMD:LED_0402_1005Metric, F.Cu at (105.4, 47.0)
- added D33: LED, LED_SMD:LED_0402_1005Metric, F.Cu at (146.9, 73.5)
- added D33: LED, LED_SMD:LED_0402_1005Metric, F.Cu at (105.4, 73.5)
- added D34: LED, LED_SMD:LED_0402_1005Metric, F.Cu at (146.9, 48.4)
- added D34: LED, LED_SMD:LED_0402_1005Metric, F.Cu at (105.4, 48.4)
- added D34: LED, LED_SMD:LED_0402_1005Metric, F.Cu at (146.9, 74.8)
- added D34: LED, LED_SMD:LED_0402_1005Metric, F.Cu at (105.4, 74.8)
- added D35: LED, LED_SMD:LED_0402_1005Metric, F.Cu at (146.9, 49.7)
- added D35: LED, LED_SMD:LED_0402_1005Metric, F.Cu at (105.4, 49.7)
- added D35: LED, LED_SMD:LED_0402_1005Metric, F.Cu at (146.9, 76.2)
- added D35: LED, LED_SMD:LED_0402_1005Metric, F.Cu at (105.4, 76.2)
- added D36: LED, LED_SMD:LED_0402_1005Metric, F.Cu at (146.9, 51.0)
- added D36: LED, LED_SMD:LED_0402_1005Metric, F.Cu at (105.4, 51.0)
- added D36: LED, LED_SMD:LED_0402_1005Metric, F.Cu at (146.9, 77.5)
- added D36: LED, LED_SMD:LED_0402_1005Metric, F.Cu at (105.4, 77.5)
- added D37: LED, LED_SMD:LED_0402_1005Metric, F.Cu at (146.9, 52.4)
- added D37: LED, LED_SMD:LED_0402_1005Metric, F.Cu at (105.4, 52.4)
- added D37: LED, LED_SMD:LED_0402_1005Metric, F.Cu at (146.9, 78.9)
- added D37: LED, LED_SMD:LED_0402_1005Metric, F.Cu at (105.4, 78.9)
- added D38: LED, LED_SMD:LED_0402_1005Metric, F.Cu at (146.9, 53.8)
- added D38: LED, LED_SMD:LED_0402_1005Metric, F.Cu at (105.4, 53.8)
- added D38: LED, LED_SMD:LED_0402_1005Metric, F.Cu at (146.9, 80.2)
- added D38: LED, LED_SMD:LED_0402_1005Metric, F.Cu at (105.4, 80.2)
- added D39: LED, LED_SMD:LED_0402_1005Metric, F.Cu at (146.9, 55.1)
- added D39: LED, LED_SMD:LED_0402_1005Metric, F.Cu at (105.4, 55.1)
- added D39: LED, LED_SMD:LED_0402_1005Metric, F.Cu at (146.9, 81.6)
- added D39: LED, LED_SMD:LED_0402_1005Metric, F.Cu at (105.4, 81.6)
- added D4: LED, LED_SMD:LED_0402_1005Metric, F.Cu at (141.5, 51.0)
- added D4: LED, LED_SMD:LED_0402_1005Metric, F.Cu at (100.0, 51.0)
- added D4: LED, LED_SMD:LED_0402_1005Metric, F.Cu at (141.5, 77.5)
- added D4: LED, LED_SMD:LED_0402_1005Metric, F.Cu at (100.0, 77.5)
- added D40: LED, LED_SMD:LED_0402_1005Metric, F.Cu at (146.9, 56.5)
- added D40: LED, LED_SMD:LED_0402_1005Metric, F.Cu at (105.4, 56.5)
- added D40: LED, LED_SMD:LED_0402_1005Metric, F.Cu at (146.9, 83.0)
- added D40: LED, LED_SMD:LED_0402_1005Metric, F.Cu at (105.4, 83.0)
- added D41: LED, LED_SMD:LED_0402_1005Metric, F.Cu at (148.2, 47.0)
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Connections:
- C1 pad 1: (no net) -> +3V0
- C1 pad 2: (no net) -> GND
- C2 pad 1: (no net) -> +3V0
- C2 pad 2: (no net) -> GND
- C3 pad 1: (no net) -> GND
- C3 pad 2: (no net) -> +3V0
- C4 pad 1: (no net) -> Net-(C4-Pad1)
- C4 pad 2: (no net) -> GND
- D1 pad 1: (no net) -> /K0
- D1 pad 2: (no net) -> /A8
- D10 pad 1: (no net) -> /K1
- D10 pad 2: (no net) -> /A8
- D11 pad 1: (no net) -> /K1
- D11 pad 2: (no net) -> /A2
- D12 pad 1: (no net) -> /K1
- D12 pad 2: (no net) -> /A3
- D13 pad 1: (no net) -> /K1
- D13 pad 2: (no net) -> /A4
- D14 pad 1: (no net) -> /K1
- D14 pad 2: (no net) -> /A5
- D15 pad 1: (no net) -> /K1
- D15 pad 2: (no net) -> /A6
- D16 pad 1: (no net) -> /K1
- D16 pad 2: (no net) -> /A7
- D17 pad 1: (no net) -> /K2
- D17 pad 2: (no net) -> /A0
- D18 pad 1: (no net) -> /K2
- D18 pad 2: (no net) -> /A1
- D19 pad 1: (no net) -> /K2
- D19 pad 2: (no net) -> /A8
- D2 pad 1: (no net) -> /K0
- D2 pad 2: (no net) -> /A1
- D20 pad 1: (no net) -> /K2
- D20 pad 2: (no net) -> /A3
- D21 pad 1: (no net) -> /K2
- D21 pad 2: (no net) -> /A4
- D22 pad 1: (no net) -> /K2
- D22 pad 2: (no net) -> /A5
- D23 pad 1: (no net) -> /K2
- D23 pad 2: (no net) -> /A6
- D24 pad 1: (no net) -> /K2
- D24 pad 2: (no net) -> /A7
- D25 pad 1: (no net) -> /K3
- D25 pad 2: (no net) -> /A0
- D26 pad 1: (no net) -> /K3
- D26 pad 2: (no net) -> /A1
- D27 pad 1: (no net) -> /K3
- D27 pad 2: (no net) -> /A2
- D28 pad 1: (no net) -> /K3
- D28 pad 2: (no net) -> /A8
- D29 pad 1: (no net) -> /K3
- D29 pad 2: (no net) -> /A4
- D3 pad 1: (no net) -> /K0
- D3 pad 2: (no net) -> /A2
- D30 pad 1: (no net) -> /K3
- D30 pad 2: (no net) -> /A5
- D31 pad 1: (no net) -> /K3
- D31 pad 2: (no net) -> /A6
- D32 pad 1: (no net) -> /K3
- D32 pad 2: (no net) -> /A7
- D33 pad 1: (no net) -> /K4
- D33 pad 2: (no net) -> /A0
- D34 pad 1: (no net) -> /K4
- D34 pad 2: (no net) -> /A1
- D35 pad 1: (no net) -> /K4
- D35 pad 2: (no net) -> /A2
- D36 pad 1: (no net) -> /K4
- D36 pad 2: (no net) -> /A3
- D37 pad 1: (no net) -> /K4
- D37 pad 2: (no net) -> /A8
- D38 pad 1: (no net) -> /K4
- D38 pad 2: (no net) -> /A5
- D39 pad 1: (no net) -> /K4
- D39 pad 2: (no net) -> /A6
- D4 pad 1: (no net) -> /K0
- D4 pad 2: (no net) -> /A3
- D40 pad 1: (no net) -> /K4
- D40 pad 2: (no net) -> /A7
- D41 pad 1: (no net) -> /K5
- D41 pad 2: (no net) -> /A0
- D42 pad 1: (no net) -> /K5
- D42 pad 2: (no net) -> /A1
- D43 pad 1: (no net) -> /K5
- D43 pad 2: (no net) -> /A2
- D44 pad 1: (no net) -> /K5
- D44 pad 2: (no net) -> /A3
- D45 pad 1: (no net) -> /K5
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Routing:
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- removed copper zone on F.Cu, net (none)
- removed copper zone on In1.Cu, net (none)
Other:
- outline, holes or cut-outs redrawn
- rule pad_to_mask_clearance: 0.05 -> 0
